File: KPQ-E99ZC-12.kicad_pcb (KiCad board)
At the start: 2 copper layers, 79 x 50.7 mm, 23 parts, among them J1 USB, J2 Chassis, J3 SWD, J4 Edge Connector, J5 Alternate Connector, SW1 BOOT, U1 USBLC6-2SC6, U2 XC6206P332MR-G, U3 STM32C071KBT6

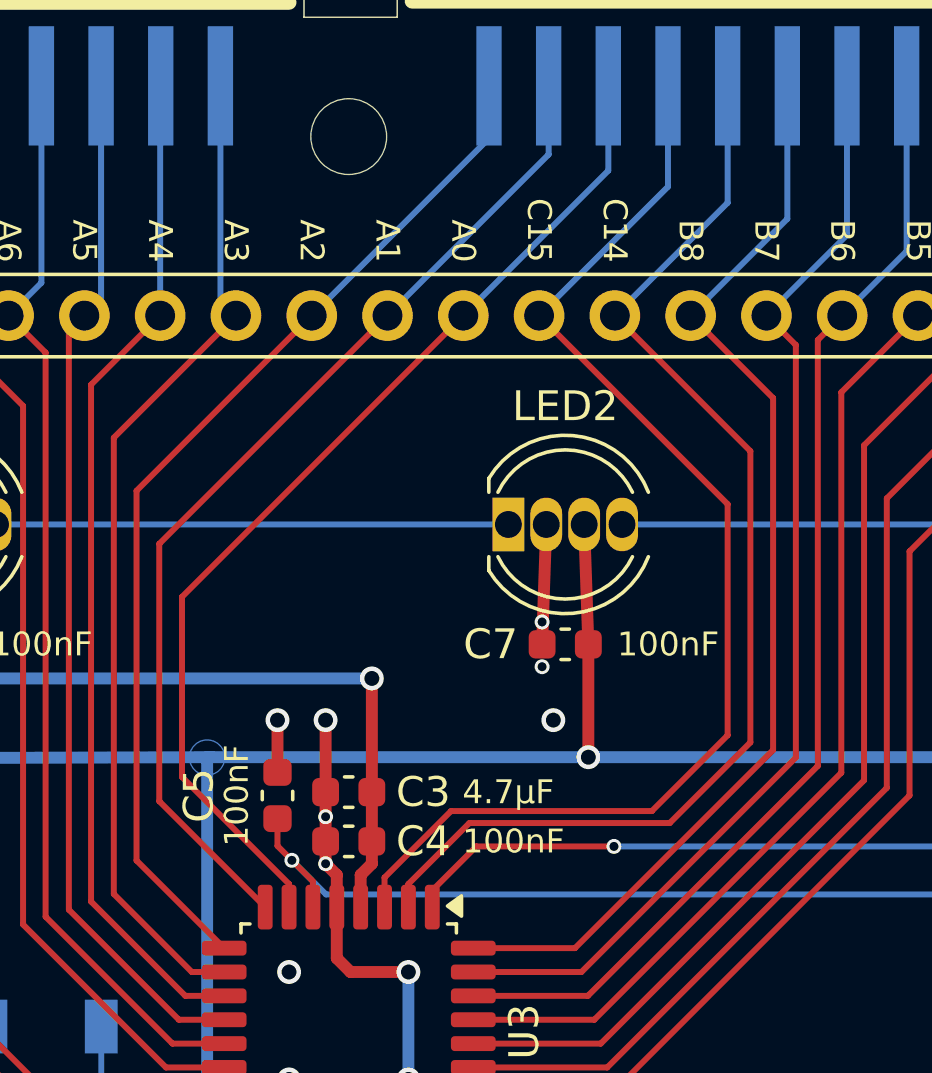
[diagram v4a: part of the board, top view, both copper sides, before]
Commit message: Support STM32G0B1KBT6 in addition to STM32C071KBT6
The pin-out is the same, but the G0B1 datasheet says that pin PC13, PC14 and PC15 should not be used as outputs. The schematic is therefore updated to move Row 8 away from PC14. This requires a little rerouting, but nothing tricky.
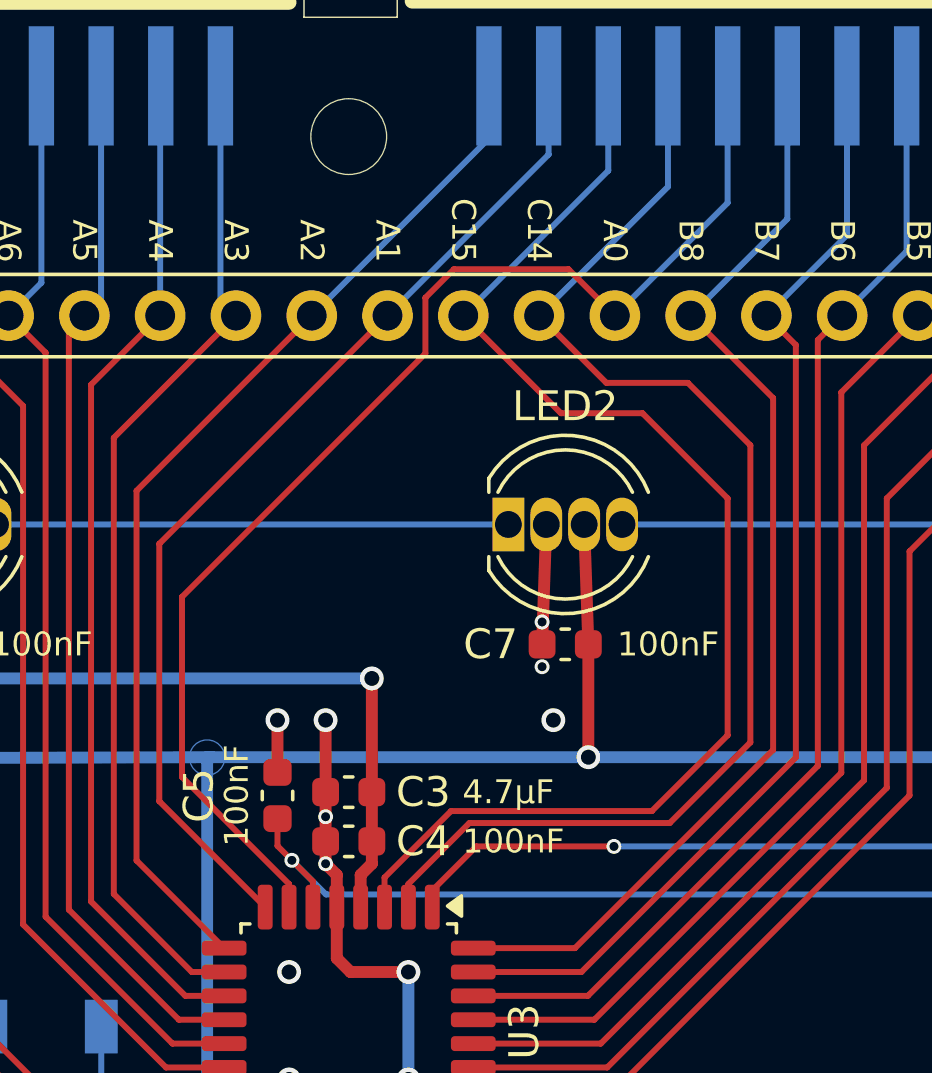
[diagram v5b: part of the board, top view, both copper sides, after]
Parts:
- U3: value STM32C071KBT6 -> STM32[C07/G0B]1KBT6
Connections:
- U3 pad 2: Row8 -> Col1
- U3 pad 3: Col1 -> Col2
- U3 pad 7: Col2 -> Row8
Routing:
- net Col2: track 34.7 -> 43.8 mm
- net Col1: track 40.9 -> 42.8 mm
- net Row8: track 40.0 -> 41.7 mm
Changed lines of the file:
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@@
 			(outputformat 1)
 			(mirror no)
-			(drillshape 1)
+			(drillshape 0)
 			(scaleselection 1)
-			(outputdirectory "")
+			(outputdirectory "Gerbers/")
 		)
 	)
@@
 			)
 		)
-		(property "Datasheet" ""
+		(property "Datasheet" "~"
 			(at 0 0 0)
 			(unlocked yes)
@@
 			)
 		)
-		(property "Datasheet" ""
+		(property "Datasheet" "~"
 			(at 0 0 90)
 			(unlocked yes)
@@
 			)
 		)
-		(property "Datasheet" ""
+		(property "Datasheet" "~"
 			(at 0 0 0)
 			(unlocked yes)
@@
 			)
 		)
-		(property "Datasheet" ""
+		(property "Datasheet" "~"
 			(at 0 0 180)
 			(unlocked yes)
@@
 			)
 		)
-		(property "Datasheet" ""
+		(property "Datasheet" "~"
 			(at 0 0 0)
 			(unlocked yes)
@@
 			)
 		)
-		(property "Datasheet" ""
+		(property "Datasheet" "~"
 			(at 0 0 0)
 			(unlocked yes)
@@
 			)
 		)
-		(property "Value" "STM32C071KBT6"
+		(property "Value" "STM32[C07/G0B]1KBT6"
 			(at 0 5.88 270)
 			(layer "F.Fab")
@@
 			(layers "F.Cu" "F.Mask" "F.Paste")
 			(roundrect_rratio 0.25)
-			(net 32 "Row8")
+			(net 23 "Col1")
 			(pinfunction "PC14")
 			(pintype "bidirectional")
@@
 			(layers "F.Cu" "F.Mask" "F.Paste")
 			(roundrect_rratio 0.25)
-			(net 23 "Col1")
+			(net 25 "Col2")
 			(pinfunction "PC15")
 			(pintype "bidirectional")
@@
 			(layers "F.Cu" "F.Mask" "F.Paste")
 			(roundrect_rratio 0.25)
-			(net 25 "Col2")
+			(net 32 "Row8")
 			(pinfunction "PA0")
 			(pintype "bidirectional")
@@
 		(tags "Through hole pin header THT 1x24 2.54mm single row")
 		(property "Reference" "J5"
-			(at 0 -2.38 270)
+			(at 0 -2.38 90)
 			(layer "F.SilkS")
 			(hide yes)
@@
 		)
 		(property "Value" "Alternate Connector"
-			(at 0 60.8 270)
+			(at 0 60.8 90)
 			(layer "F.Fab")
 			(effects
@@
 			)
 		)
-		(property "Datasheet" ""
-			(at 0 0 270)
+		(property "Datasheet" "~"
+			(at 0 0 90)
 			(layer "F.Fab")
 			(hide yes)
@@
 		)
 		(property "Description" "Generic connector, single row, 01x24, script generated (kicad-library-utils/schlib/autogen/connector/)"
-			(at 0 0 270)
+			(at 0 0 90)
 			(layer "F.Fab")
 			(hide yes)
@@
 			)
 		)
-		(property "P8" "C14"
+		(property "P8" "A0"
 			(at 0 0 270)
 			(unlocked yes)
@@
 			)
 		)
-		(property "P9" "C15"
+		(property "P9" "C14"
 			(at 0 0 270)
 			(unlocked yes)
@@
 			)
 		)
-		(property "P10" "A0"
+		(property "P10" "C15"
 			(at 0 0 270)
 			(unlocked yes)
@@
 			)
 		)
-		(property "Datasheet" ""
+		(property "Datasheet" "~"
 			(at 0 0 90)
 			(unlocked yes)
@@
 			)
 		)
-		(property "Datasheet" ""
+		(property "Datasheet" "~"
 			(at 0 0 270)
 			(unlocked yes)
@@
 			)
 		)
-		(property "Datasheet" ""
+		(property "Datasheet" "~"
 			(at 0 0 0)
 			(unlocked yes)
@@
 			)
 		)
-		(property "Datasheet" ""
+		(property "Datasheet" "~"
 			(at 0 0 180)
 			(unlocked yes)
@@
 			)
 		)
-		(property "Datasheet" ""
+		(property "Datasheet" "~"
 			(at 0 0 0)
 			(unlocked yes)
@@
 			)
 		)
-		(property "Datasheet" ""
+		(property "Datasheet" "~"
 			(at 0 0 180)
 			(unlocked yes)
@@
 			)
 		)
-		(property "Datasheet" ""
+		(property "Datasheet" "~"
 			(at 0 0 180)
 			(layer "F.Fab")
@@
 			)
 		)
-		(property "Datasheet" ""
+		(property "Datasheet" "~"
 			(at 0 0 180)
 			(unlocked yes)
@@
 			)
 		)
-		(property "Datasheet" ""
+		(property "Datasheet" "~"
 			(at 0 0 270)
 			(unlocked yes)
@@
 			)
 		)
-		(property "Datasheet" ""
+		(property "Datasheet" "~"
 			(at 0 2 0)
 			(unlocked yes)
@@
 	)
 	(segment
-		(start 101.2 125.825)
-		(end 101.2 124.835)
+		(start 113.462 120.3052)
+		(end 113.462 110.348)
 		(width 0.2)
 		(layer "F.Cu")
@@
 	)
 	(segment
-		(start 112.7 112.32)
-		(end 106.38 106)
+		(start 102 125.825)
+		(end 102 125.051)
 		(width 0.2)
 		(layer "F.Cu")
@@
 	)
 	(segment
-		(start 103.429 122.606)
-		(end 110.16 122.606)
+		(start 111.369 108.255)
+		(end 108.635 108.255)
 		(width 0.2)
 		(layer "F.Cu")
@@
 	)
 	(segment
-		(start 110.16 122.606)
-		(end 112.7 120.066)
+		(start 110.7602 123.007)
+		(end 113.462 120.3052)
 		(width 0.2)
 		(layer "F.Cu")
@@
 	)
 	(segment
-		(start 101.2 124.835)
-		(end 103.429 122.606)
+		(start 108.635 108.255)
+		(end 106.38 106)
 		(width 0.2)
 		(layer "F.Cu")
@@
 	)
 	(segment
-		(start 112.7 120.066)
-		(end 112.7 112.32)
+		(start 102 125.051)
+		(end 104.044 123.007)
+		(width 0.2)
+		(layer "F.Cu")
+		(net 23)
+	)
+	(segment
+		(start 104.044 123.007)
+		(end 110.7602 123.007)
+		(width 0.2)
+		(layer "F.Cu")
+		(net 23)
+	)
+	(segment
+		(start 113.462 110.348)
+		(end 111.369 108.255)
 		(width 0.2)
 		(layer "F.Cu")
@@
 	)
 	(segment
-		(start 98 125.269082)
-		(end 98 125.051)
+		(start 112.7 112.126)
+		(end 109.845 109.271)
 		(width 0.2)
 		(layer "F.Cu")
@@
 	)
 	(segment
-		(start 94.412 121.463)
-		(end 94.412 115.428)
+		(start 101.2 124.835)
+		(end 103.429 122.606)
 		(width 0.2)
 		(layer "F.Cu")
@@
 	)
 	(segment
-		(start 98 125.051)
-		(end 94.412 121.463)
+		(start 110.16 122.606)
+		(end 112.7 120.066)
 		(width 0.2)
 		(layer "F.Cu")
@@
 	)
 	(segment
-		(start 94.412 115.428)
+		(start 109.845 109.271)
+		(end 107.111 109.271)
+		(width 0.2)
+		(layer "F.Cu")
+		(net 25)
+	)
+	(segment
+		(start 101.2 125.825)
+		(end 101.2 124.835)
+		(width 0.2)
+		(layer "F.Cu")
+		(net 25)
+	)
+	(segment
+		(start 107.111 109.271)
 		(end 103.84 106)
 		(width 0.2)
@@
 	)
 	(segment
+		(start 103.429 122.606)
+		(end 110.16 122.606)
+		(width 0.2)
+		(layer "F.Cu")
+		(net 25)
+	)
+	(segment
+		(start 112.7 120.066)
+		(end 112.7 112.126)
+		(width 0.2)
+		(layer "F.Cu")
+		(net 25)
+	)
+	(segment
 		(start 103.84 106)
 		(end 108.7 101.14)
@@
 	)
 	(segment
-		(start 102 125.051)
-		(end 104.044 123.007)
+		(start 107.365 104.445)
+		(end 103.526 104.445)
 		(width 0.2)
 		(layer "F.Cu")
@@
 	)
 	(segment
-		(start 104.044 123.007)
-		(end 110.7602 123.007)
+		(start 98 125.051)
+		(end 98 125.269082)
 		(width 0.2)
 		(layer "F.Cu")
@@
 	)
 	(segment
-		(start 113.462 110.542)
-		(end 108.92 106)
+		(start 102.57 107.27)
+		(end 94.412 115.428)
 		(width 0.2)
 		(layer "F.Cu")
@@
 	)
 	(segment
-		(start 113.462 120.3052)
-		(end 113.462 110.542)
+		(start 108.92 106)
+		(end 107.365 104.445)
 		(width 0.2)
 		(layer "F.Cu")
@@
 	)
 	(segment
-		(start 110.7602 123.007)
-		(end 113.462 120.3052)
+		(start 102.57 105.401)
+		(end 102.57 107.27)
 		(width 0.2)
 		(layer "F.Cu")
@@
 	)
 	(segment
-		(start 102 125.825)
-		(end 102 125.051)
+		(start 94.412 121.463)
+		(end 98 125.051)
+		(width 0.2)
+		(layer "F.Cu")
+		(net 32)
+	)
+	(segment
+		(start 103.526 104.445)
+		(end 102.57 105.401)
+		(width 0.2)
+		(layer "F.Cu")
+		(net 32)
+	)
+	(segment
+		(start 94.412 115.428)
+		(end 94.412 121.463)
 		(width 0.2)
 		(layer "F.Cu")

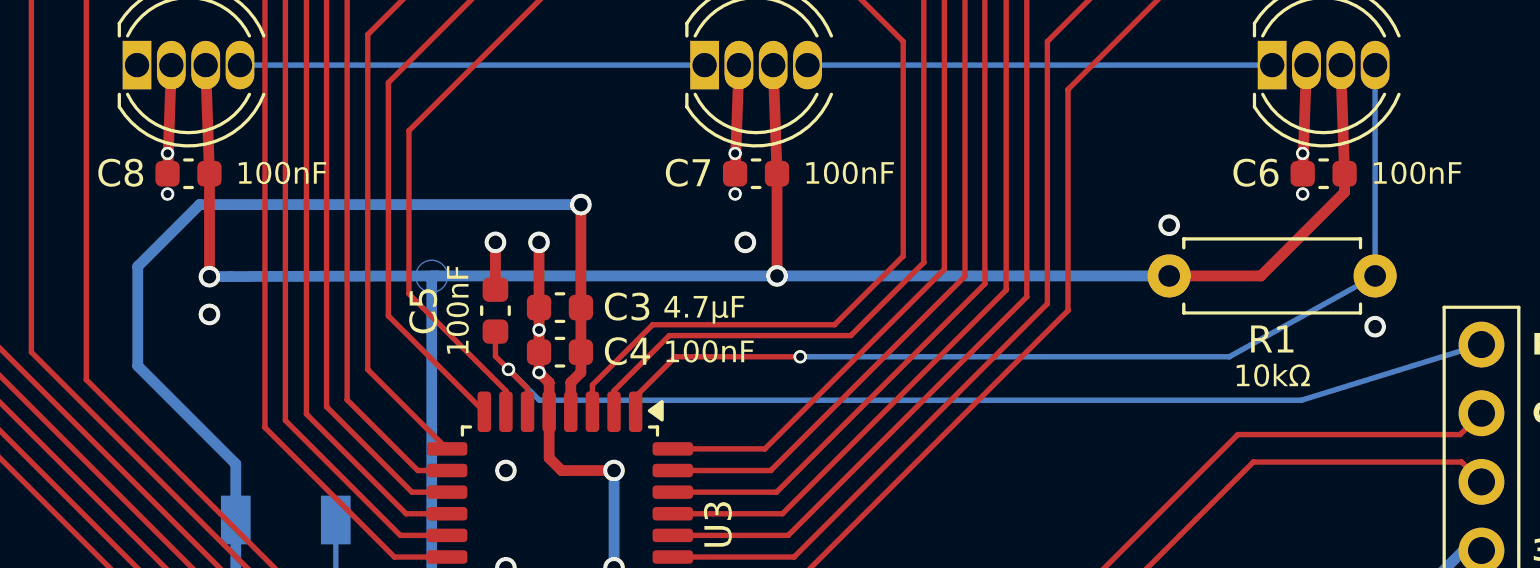
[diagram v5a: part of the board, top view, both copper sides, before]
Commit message: Change R1 to combined THT/SMT footprint
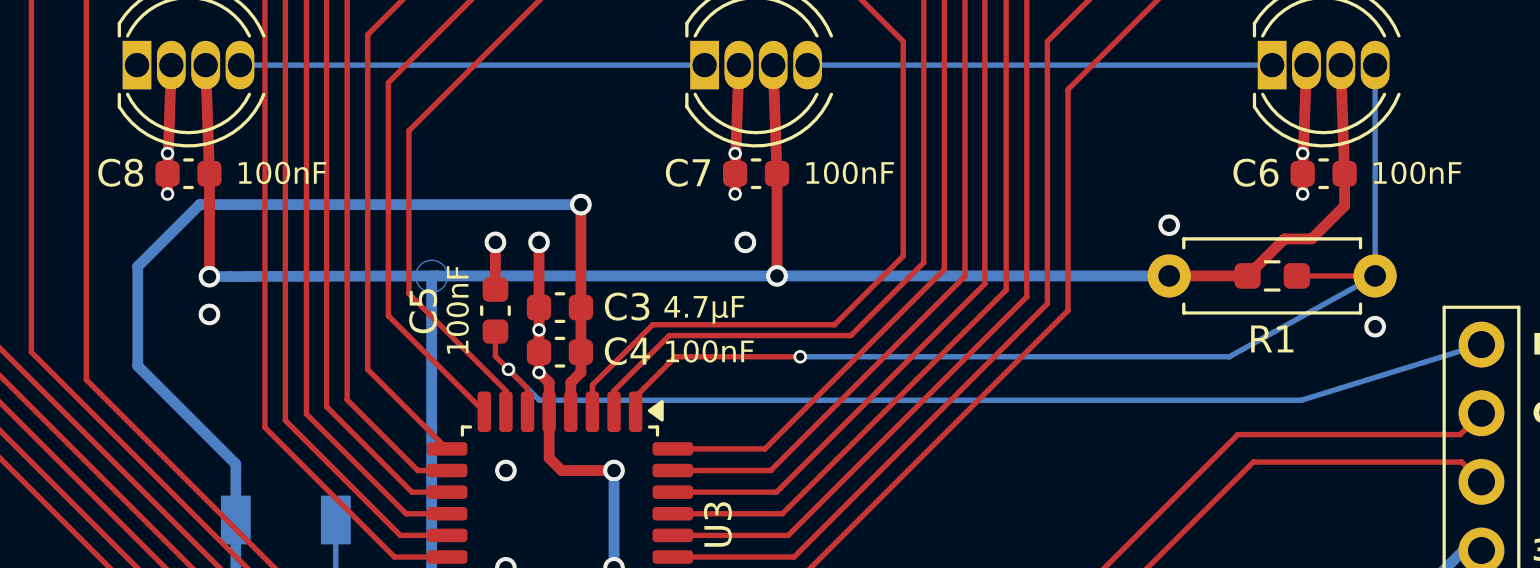
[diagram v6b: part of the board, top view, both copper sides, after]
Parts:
- R1: footprint Resistor_THT:R_Axial_DIN0207_L6.3mm_D2.5mm_P7.62mm_Horizontal -> BGK_Kicad:R_Combined_Axial_DIN0207_0603_1608Metric
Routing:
- net LED: track 36.5 -> 39.4 mm
- net GND: track 65.3 -> 67.6 mm
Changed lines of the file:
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@@
 		)
 	)
-	(footprint "Resistor_THT:R_Axial_DIN0207_L6.3mm_D2.5mm_P7.62mm_Horizontal"
+	(footprint "BGK_Kicad:R_Combined_Axial_DIN0207_0603_1608Metric"
 		(layer "F.Cu")
 		(at 130.161 120.8 180)
-		(descr "Resistor, Axial_DIN0207 series, Axial, Horizontal, pin pitch=7.62mm, 0.25W = 1/4W, length*diameter=6.3*2.5mm^2, http://cdn-reichelt.de/documents/datenblatt/B400/1_4W%23YAG.pdf")
-		(tags "Resistor Axial_DIN0207 series Axial Horizontal pin pitch 7.62mm 0.25W = 1/4W length 6.3mm diameter 2.5mm")
+		(descr "Resistor, combined Axial_DIN0207 series and SMD 0603 (1608 Metric); Axial: Horizontal, pin pitch=7.62mm, 0.25W = 1/4W, length*diameter=6.3*2.5mm^2, SMD: square (rectangular) end terminal, IPC-7351 nominal, generated with kicad-footprint-generator")
+		(tags "resistor")
 		(property "Reference" "R1"
 			(at 3.81 -2.37 180)
@@
 		)
 		(property "Value" "10kΩ"
-			(at 3.81 -3.711 180)
-			(layer "F.SilkS")
+			(at 3.81 2.37 180)
+			(layer "F.Fab")
 			(effects
 				(font
-					(size 0.8 0.8)
-					(thickness 0.1)
+					(size 1 1)
+					(thickness 0.15)
 				)
 			)
@@
 		(property "Datasheet" "~"
 			(at 0 0 180)
-			(unlocked yes)
 			(layer "F.Fab")
 			(hide yes)
@@
 		(property "Description" "Resistor"
 			(at 0 0 180)
-			(unlocked yes)
 			(layer "F.Fab")
 			(hide yes)
@@
 		)
 		(fp_line
-			(start 0.54 1.37)
-			(end 7.08 1.37)
+			(start 3.555276 0.5225)
+			(end 4.064724 0.5225)
 			(stroke
 				(width 0.12)
@@
 		)
 		(fp_line
-			(start 0.54 1.04)
-			(end 0.54 1.37)
+			(start 3.555276 -0.5225)
+			(end 4.064724 -0.5225)
 			(stroke
 				(width 0.12)
@@
 		)
 		(fp_line
-			(start 0.54 -1.04)
-			(end 0.54 -1.37)
+			(start 0.54 1.37)
+			(end 7.08 1.37)
 			(stroke
 				(width 0.12)
@@
 		)
 		(fp_line
-			(start 0.54 -1.37)
-			(end 7.08 -1.37)
+			(start 0.54 1.04)
+			(end 0.54 1.37)
 			(stroke
 				(width 0.12)
@@
 		)
 		(fp_line
-			(start 8.67 1.5)
-			(end 8.67 -1.5)
-			(stroke
-				(width 0.05)
-				(type solid)
-			)
-			(layer "F.CrtYd")
-		)
-		(fp_line
-			(start 8.67 -1.5)
-			(end -1.05 -1.5)
+			(start 0.54 -1.04)
+			(end 0.54 -1.37)
 			(stroke
-				(width 0.05)
+				(width 0.12)
 				(type solid)
 			)
-			(layer "F.CrtYd")
+			(layer "F.SilkS")
 		)
 		(fp_line
-			(start -1.05 1.5)
-			(end 8.67 1.5)
+			(start 0.54 -1.37)
+			(end 7.08 -1.37)
 			(stroke
-				(width 0.05)
+				(width 0.12)
 				(type solid)
 			)
-			(layer "F.CrtYd")
+			(layer "F.SilkS")
 		)
-		(fp_line
+		(fp_rect
 			(start -1.05 -1.5)
-			(end -1.05 1.5)
+			(end 8.67 1.5)
 			(stroke
 				(width 0.05)
 				(type solid)
 			)
+			(fill no)
 			(layer "F.CrtYd")
 		)
@@
 		)
 		(fp_line
-			(start 6.96 1.25)
-			(end 6.96 -1.25)
+			(start 4.61 0.4125)
+			(end 3.01 0.4125)
 			(stroke
 				(width 0.1)
@@
 		)
 		(fp_line
-			(start 6.96 -1.25)
-			(end 0.66 -1.25)
+			(start 4.61 -0.4125)
+			(end 4.61 0.4125)
 			(stroke
 				(width 0.1)
@@
 		)
 		(fp_line
-			(start 0.66 1.25)
-			(end 6.96 1.25)
+			(start 3.01 0.4125)
+			(end 3.01 -0.4125)
 			(stroke
 				(width 0.1)
@@
 		)
 		(fp_line
-			(start 0.66 -1.25)
-			(end 0.66 1.25)
+			(start 3.01 -0.4125)
+			(end 4.61 -0.4125)
 			(stroke
 				(width 0.1)
@@
 			(layer "F.Fab")
 		)
+		(fp_rect
+			(start 0.66 -1.25)
+			(end 6.96 1.25)
+			(stroke
+				(width 0.1)
+				(type solid)
+			)
+			(fill no)
+			(layer "F.Fab")
+		)
 		(fp_text user "${REFERENCE}"
 			(at 3.81 0 180)
@@
 			(pintype "passive")
 		)
-		(pad "2" thru_hole oval
+		(pad "1" smd roundrect
+			(at 2.8975 0 180)
+			(size 0.975 0.95)
+			(layers "F.Cu" "F.Mask" "F.Paste")
+			(roundrect_rratio 0.25)
+			(net 34 "LED")
+			(pintype "passive")
+		)
+		(pad "2" smd roundrect
+			(at 4.7225 0 180)
+			(size 0.975 0.95)
+			(layers "F.Cu" "F.Mask" "F.Paste")
+			(roundrect_rratio 0.25)
+			(net 2 "+5V")
+			(pintype "passive")
+		)
+		(pad "2" thru_hole circle
 			(at 7.62 0 180)
 			(size 1.6 1.6)
@@
 		)
 		(embedded_fonts no)
-		(model "${KICAD9_3DMODEL_DIR}/Resistor_THT.3dshapes/R_Axial_DIN0207_L6.3mm_D2.5mm_P7.62mm_Horizontal.wrl"
+		(model "${KICAD9_3DMODEL_DIR}/Resistor_THT.3dshapes/R_Axial_DIN0207_L6.3mm_D2.5mm_P7.62mm_Horizontal.step"
 			(offset
 				(xyz 0 0 0)
@@
 	)
 	(segment
+		(start 106.481 117.018)
+		(end 106.481 117.768)
+		(width 0.4)
+		(layer "F.Cu")
+		(net 1)
+	)
+	(segment
 		(start 99.6 124.747)
 		(end 99.6 125.825)
@@
 	)
 	(segment
+		(start 85.481 117.018)
+		(end 85.481 117.768)
+		(width 0.4)
+		(layer "F.Cu")
+		(net 1)
+	)
+	(segment
 		(start 123.28 140.238355)
 		(end 124.508 139.010355)
@@
 	)
 	(segment
+		(start 127.481 117.018)
+		(end 127.481 117.768)
+		(width 0.4)
+		(layer "F.Cu")
+		(net 1)
+	)
+	(segment
 		(start 100.06 128)
 		(end 102 128)
@@
 	)
 	(segment
+		(start 122.541 120.8)
+		(end 125.4385 120.8)
+		(width 0.4)
+		(layer "F.Cu")
+		(net 2)
+	)
+	(segment
 		(start 126.114 142.810355)
 		(end 124.3935 142.810355)
@@
 	)
 	(segment
-		(start 123.255905 144.13955)
-		(end 123.255905 143.31045)
+		(start 129.031 118.213)
+		(end 129.031 117.018)
 		(width 0.4)
 		(layer "F.Cu")
@@
 	)
 	(segment
-		(start 129.031 117.018)
-		(end 128.891 113)
+		(start 123.255905 144.13955)
+		(end 123.255905 143.31045)
 		(width 0.4)
 		(layer "F.Cu")
@@
 	)
 	(segment
-		(start 129.031 117.705)
-		(end 129.031 117.018)
+		(start 129.031 117.018)
+		(end 128.891 113)
 		(width 0.4)
 		(layer "F.Cu")
@@
 	)
 	(segment
-		(start 122.541 120.8)
-		(end 125.936 120.8)
+		(start 123.255905 143.31045)
+		(end 123.756 142.810355)
 		(width 0.4)
 		(layer "F.Cu")
@@
 	)
 	(segment
-		(start 123.255905 143.31045)
-		(end 123.756 142.810355)
+		(start 126.8075 119.431)
+		(end 127.813 119.431)
 		(width 0.4)
 		(layer "F.Cu")
@@
 	)
 	(segment
-		(start 102.286 145)
-		(end 102.286 144.831)
+		(start 125.4385 120.8)
+		(end 126.8075 119.431)
 		(width 0.4)
 		(layer "F.Cu")
@@
 	)
 	(segment
-		(start 99.8675 145)
-		(end 102.286 145)
+		(start 127.813 119.431)
+		(end 129.031 118.213)
 		(width 0.4)
 		(layer "F.Cu")
@@
 	)
 	(segment
-		(start 125.936 120.8)
-		(end 129.031 117.705)
+		(start 102.286 145)
+		(end 102.286 144.831)
+		(width 0.4)
+		(layer "F.Cu")
+		(net 2)
+	)
+	(segment
+		(start 99.8675 145)
+		(end 102.286 145)
 		(width 0.4)
 		(layer "F.Cu")
@@
 	)
 	(segment
+		(start 127.2635 120.8)
+		(end 130.161 120.8)
+		(width 0.2)
+		(layer "F.Cu")
+		(net 34)
+	)
+	(segment

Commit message: Tweak routing
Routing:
- net Col10: track 44.4 -> 48.0 mm
- net Col11: track 46.2 -> 48.7 mm
- net Col12: track 49.5 -> 51.0 mm
- net Col2: track 43.8 -> 44.7 mm
- net Row8: track 41.7 -> 41.1 mm
- net Col6: track 34.3 -> 33.7 mm
- net Col5: track 33.3 -> 32.7 mm
- net Col4: track 33.2 -> 32.6 mm
- net Col3: track 34.7 -> 34.1 mm
- net GND: vias 26 -> 27
